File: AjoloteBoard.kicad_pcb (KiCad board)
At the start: 2 copper layers, 69 x 84.9 mm, 10 parts, among them SW1 On

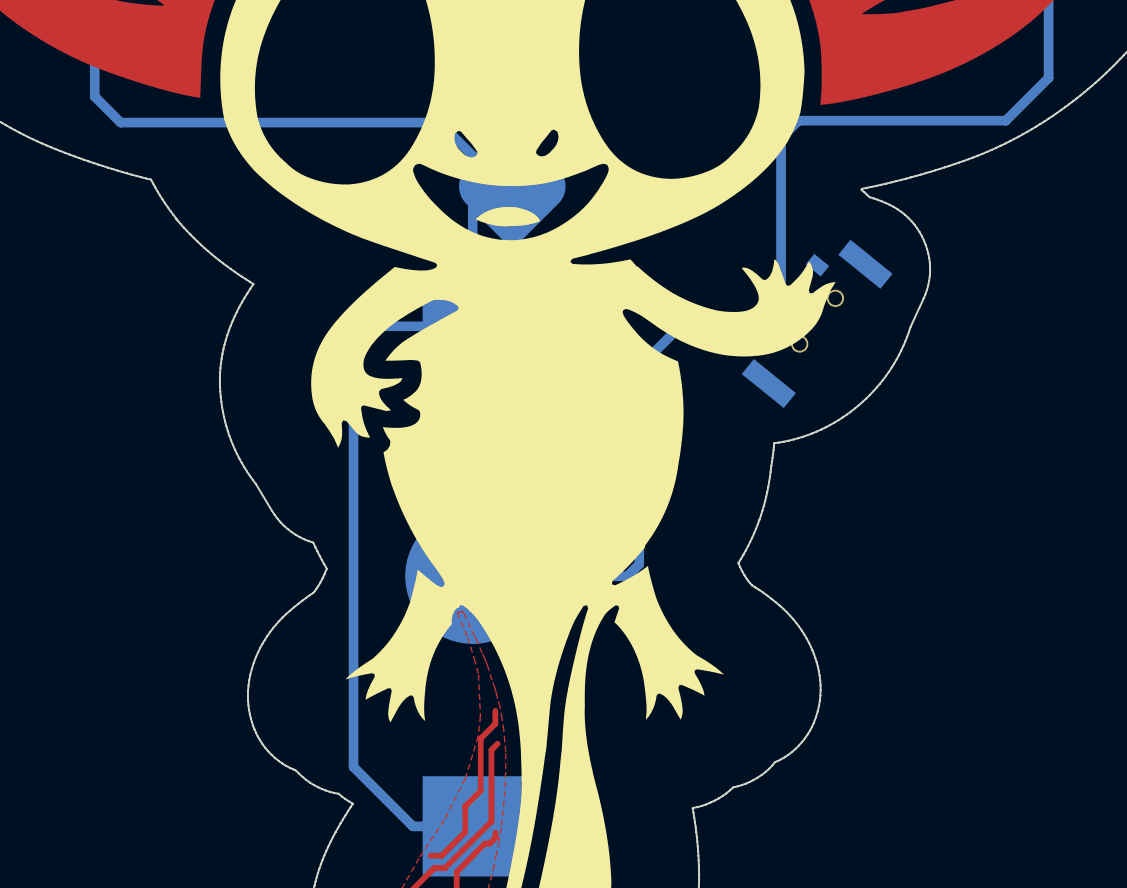
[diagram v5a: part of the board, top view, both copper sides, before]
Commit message: add wurth switch
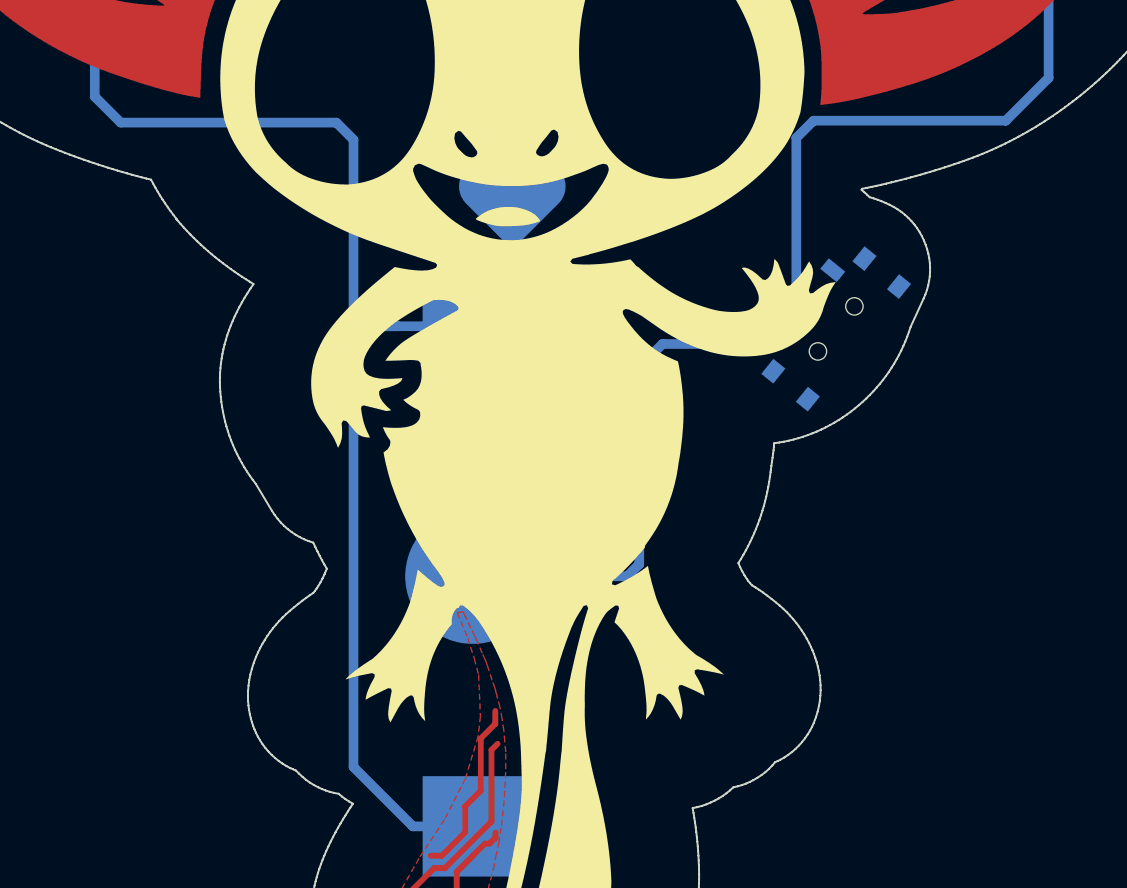
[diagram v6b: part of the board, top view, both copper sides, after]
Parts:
- SW1: footprint footprints:Micro_interruptor_SPDT -> footprints:450404015514
- moved SW1 3.48 mm to (175.6, 95.2), turned to 51 degrees
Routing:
- net Net-(BT1-Pad2): track 26.2 -> 26.9 mm
- net Net-(D1-Pad1): track 125.4 -> 124.9 mm
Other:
- board text added: "SW1"

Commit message: Add logo de PCBWay
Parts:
- added G***: LOGO, Aesthetics:pcbway, B.Cu at (137.9, 79.5)
- moved G*** 4.90 mm to (136.8, 70.8)
